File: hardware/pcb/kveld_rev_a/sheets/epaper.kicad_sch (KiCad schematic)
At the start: 0 parts

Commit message: feat(hw): capture rev a schematic and refine enclosure
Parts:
- added C12: 1uF, Capacitor_SMD:C_0603_1608Metric, symbol Device:C
- added C13: 10uF, Capacitor_SMD:C_0603_1608Metric, symbol Device:C
- added C14: 1nF, Capacitor_SMD:C_0603_1608Metric, symbol Device:C
- added C15, C16: 4.7uF 25V, Capacitor_SMD:C_0805_2012Metric, symbol Device:C
- added C17, C18, C19, C20, C22, C23, C24: 1uF 25V, Capacitor_SMD:C_0603_1608Metric, symbol Device:C
- added C21: 1nF 25V, Capacitor_SMD:C_0603_1608Metric, symbol Device:C
- added D1, D2, D3: MBR0530, Diode_SMD:D_SOD-123, symbol Device:D_Schottky
- added J2: FH12-24S-0.5SH, Connector_FFC-FPC:Hirose_FH12-24S-0.5SH_1x24-1MP_P0.50mm_Horizontal, symbol Connector_Generic:Conn_01x24
- added L1: 47uH VLS4012CX-470M-1, symbol Device:L
- added Q1: Si1308EDL, Package_TO_SOT_SMD:SOT-323_SC-70, symbol Transistor_FET:Q_NMOS_SGD
- added R18: 150, Resistor_SMD:R_0603_1608Metric, symbol Device:R
- added R19: 1M, Resistor_SMD:R_0603_1608Metric, symbol Device:R
- added R20: 2.2, Resistor_SMD:R_0603_1608Metric, symbol Device:R
- added U6: TPS22917DBVR, Package_TO_SOT_SMD:SOT-23-6, symbol Power_Management:TPS22917DBV
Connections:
- new net 3V3: C12.1, U6.1 (VIN)
- new net EPD_3V3: C13.1, C15.1, C19.1, J2.15 (Pin_15), J2.16 (Pin_16), L1.1, R18.2, U6.6 (VOUT)
- new net EPD_BUSY: J2.9 (Pin_9)
- new net EPD_CLK: J2.13 (Pin_13)
- new net EPD_CS: J2.12 (Pin_12)
- new net EPD_DC: J2.11 (Pin_11)
- new net EPD_GDR: J2.2 (Pin_2), Q1.2 (G), R19.1
- new net EPD_MOSI: J2.14 (Pin_14)
- new net EPD_NEGPUMP: C16.1, D1.1 (K), D2.2 (A)
- new net EPD_PREVGH: C17.1, D3.1 (K), J2.21 (Pin_21)
- new net EPD_PREVGL: C23.1, D1.2 (A), J2.23 (Pin_23)
- new net EPD_PWR_EN: U6.3 (ON)
- new net EPD_QOD: R18.1, U6.5 (QOD)
- new net EPD_RESE: J2.3 (Pin_3), Q1.1 (S), R20.1
- new net EPD_RESET: J2.10 (Pin_10)
- new net EPD_SW: C16.2, D3.2 (A), L1.2, Q1.3 (D)
- new net EPD_SW_CT: C14.1, U6.4 (CT)
- new net EPD_VCOM: C24.1, J2.24 (Pin_24)
- new net EPD_VDD: C20.1, J2.18 (Pin_18)
- new net EPD_VSH1: C21.1, J2.20 (Pin_20)
- new net EPD_VSH2: C18.1, J2.5 (Pin_5)
- new net EPD_VSL: C22.1, J2.22 (Pin_22)
- new net GND: C12.2, C13.2, C14.2, C15.2, C17.2, C18.2, C19.2, C20.2, C21.2, C22.2, C23.2, C24.2, D2.1 (K), J2.17 (Pin_17), J2.8 (Pin_8), R19.2, R20.2, U6.2 (GND)
- no-connect marks 0 -> 5
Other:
- note added: "The load switch removes panel and boost power between refreshes. Boost network follows Good Display's reference."
- title: (none) -> GDEY0213B74 e-paper interface and boost

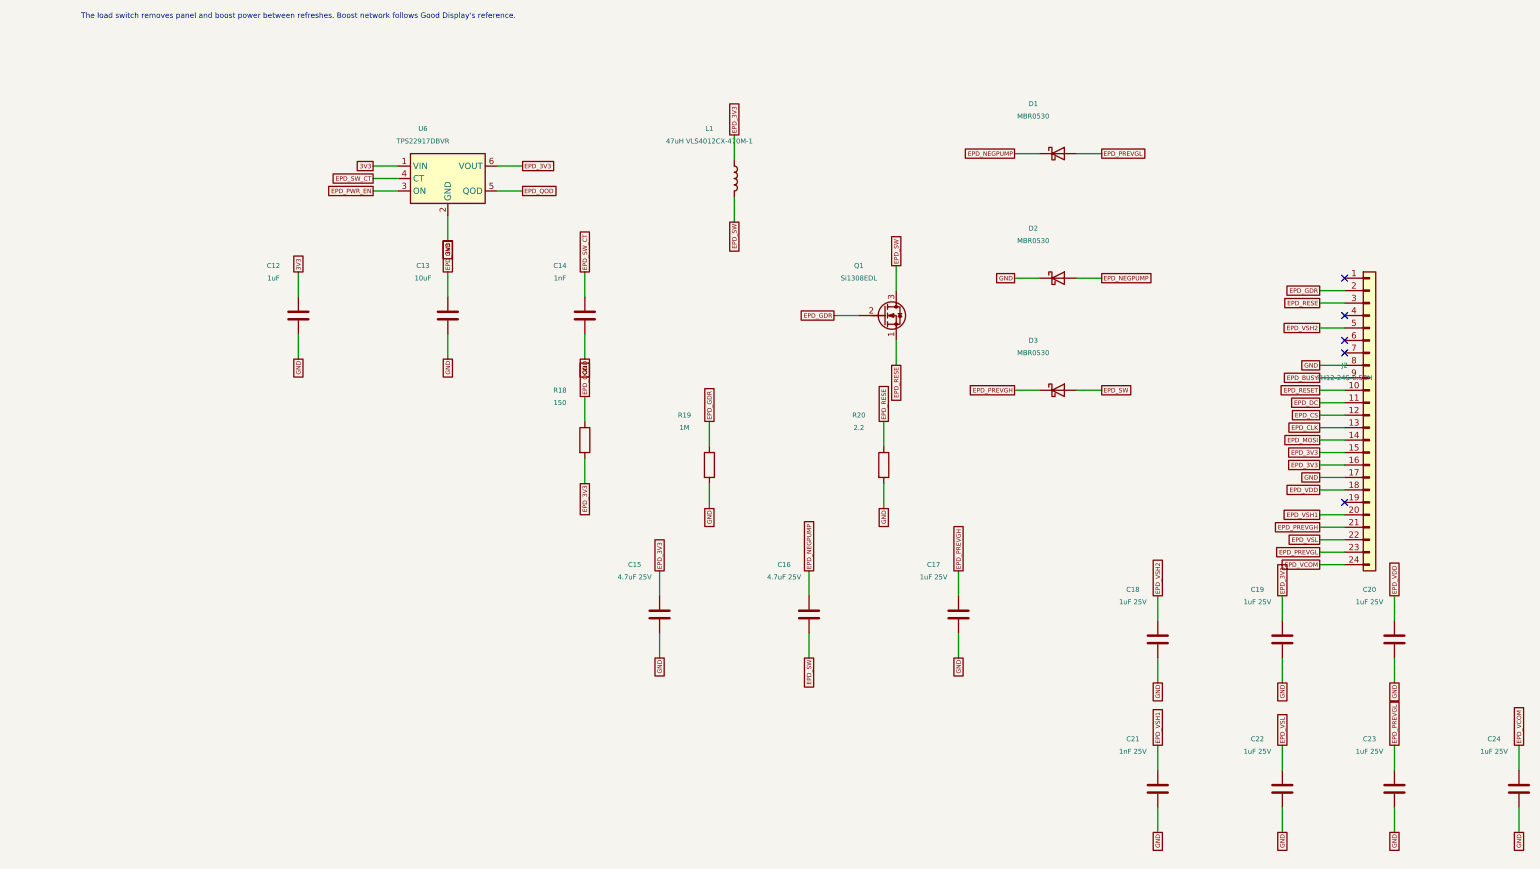
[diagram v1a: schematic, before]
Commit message: refactor(hw): consolidate and clarify schematic
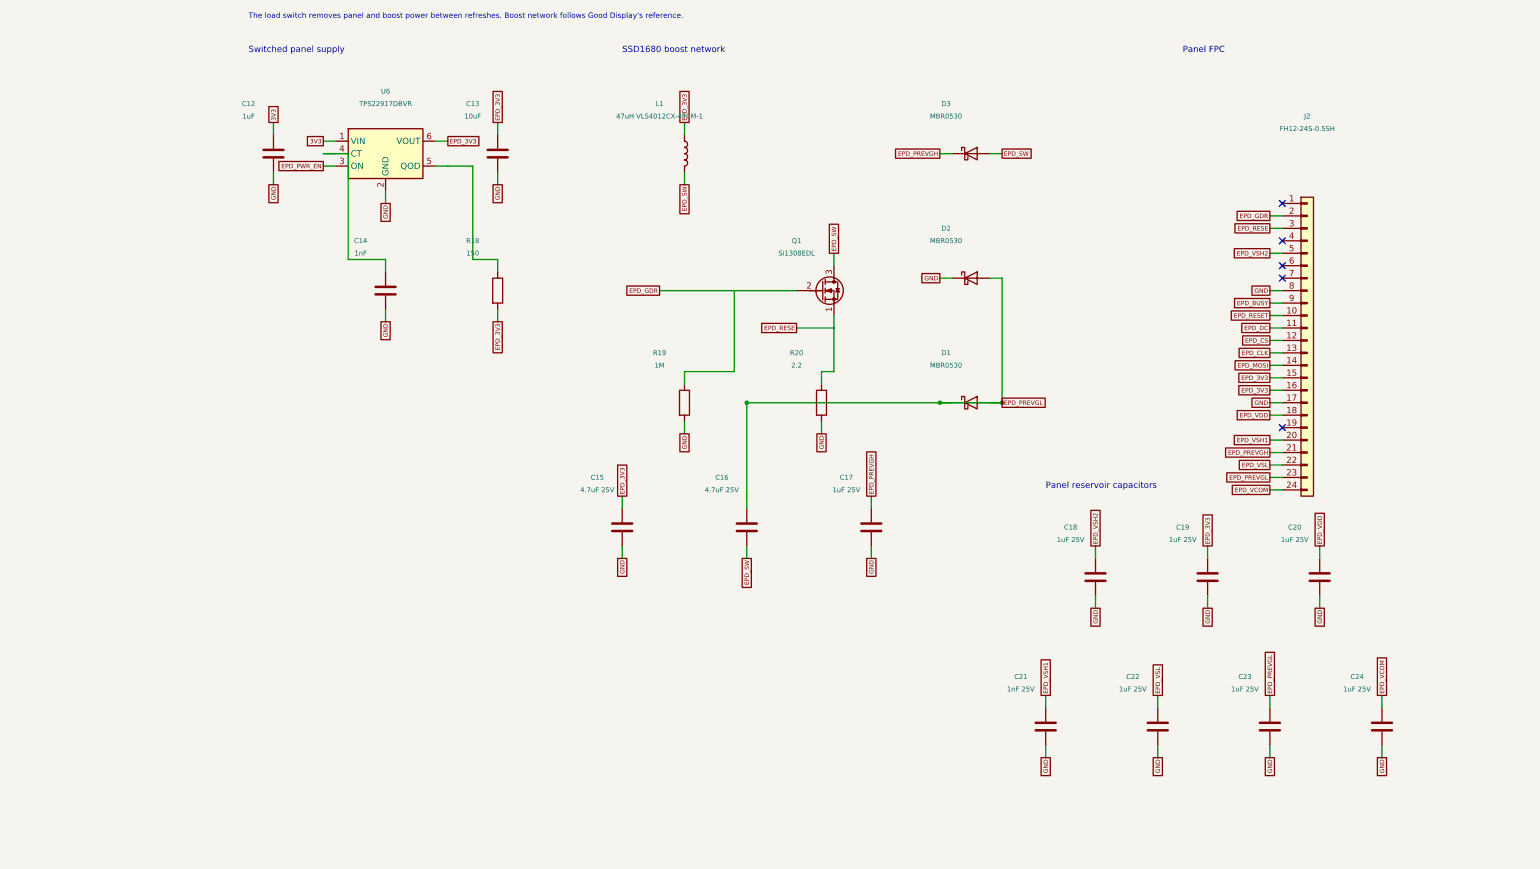
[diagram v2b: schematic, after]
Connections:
- net EPD_NEGPUMP is gone; now on net EPD_PREVGL: C16.1, D1.1 (K), D2.2 (A)
- net EPD_QOD: no longer names the net of R18.1, U6.5 (QOD)
- net EPD_SW_CT: no longer names the net of C14.1, U6.4 (CT)
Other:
- note added: "Panel FPC"
- note added: "Panel reservoir capacitors"
- note added: "SSD1680 boost network"
- note added: "Switched panel supply"
